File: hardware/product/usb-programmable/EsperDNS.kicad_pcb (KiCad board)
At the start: 4 copper layers, 51 x 48 mm, 53 parts, among them J1 USB_B_Micro, J3 RJ45_Amphenol_RJMG1BD3B8K1ANR, Q1 2N7002, Q2 2N7002, Q3 2N7002, Q4 2N7002, Q5 2N7002, SW1 PTS645VH83-2 LFS, U1 AZ1117EH-3.3TRG1, U2 ESP32-WROOM-32E, U3 LAN8720A, U4 CP2102-GMR_NRND

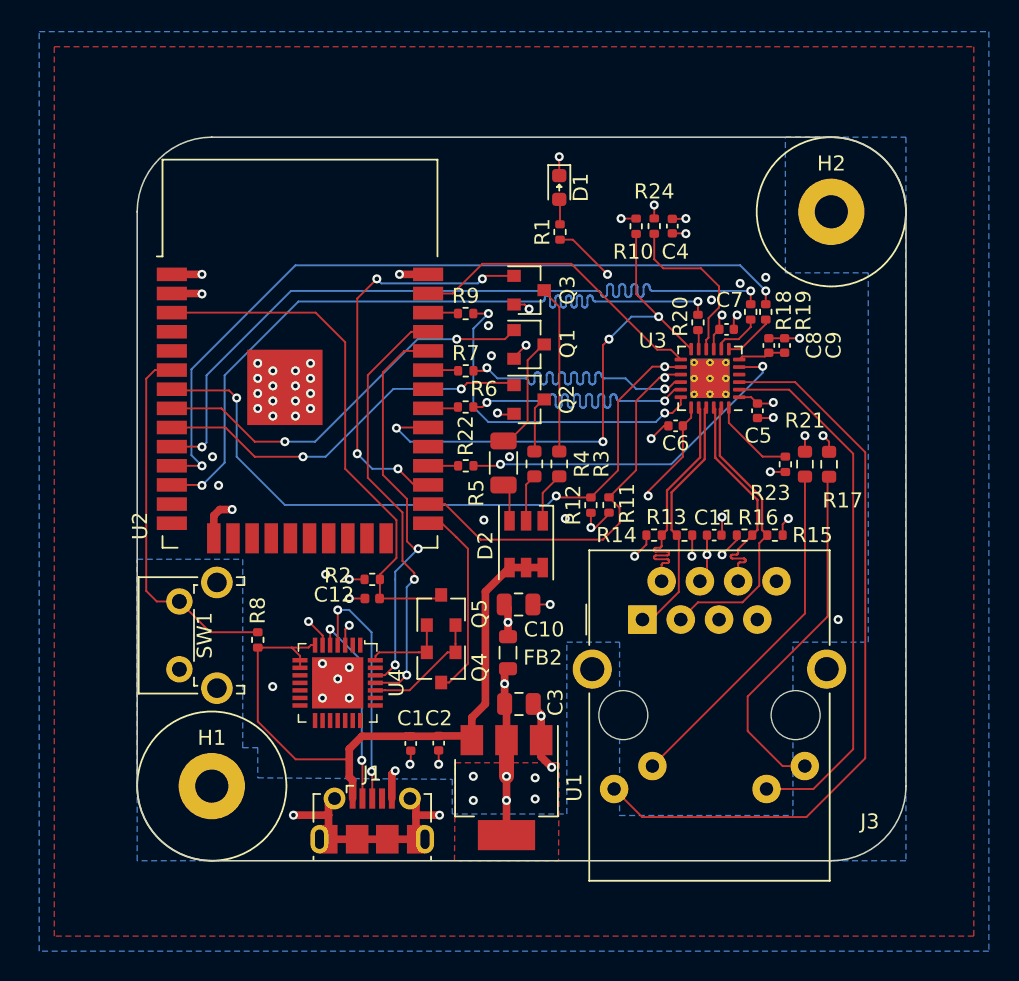
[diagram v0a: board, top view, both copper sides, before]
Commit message: Changed to new PHY
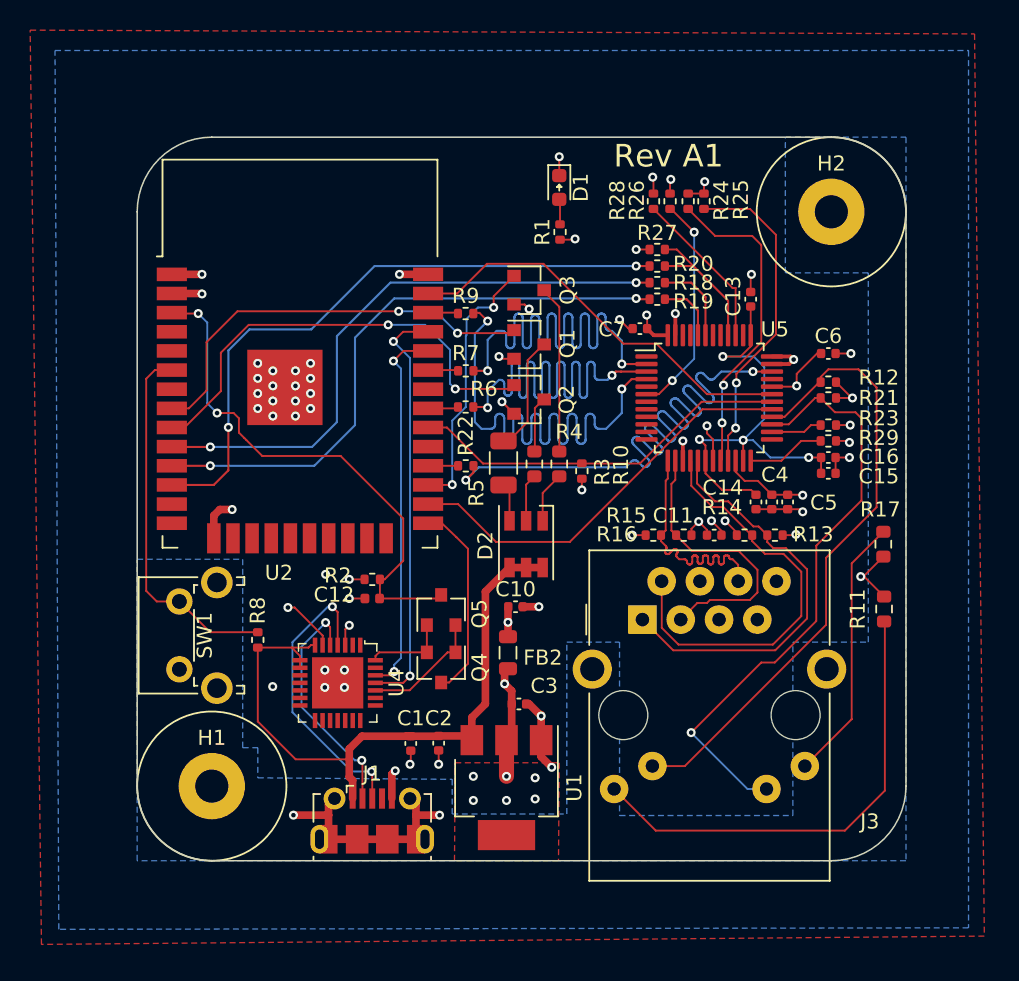
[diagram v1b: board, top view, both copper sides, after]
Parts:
- removed C8: 0.1uF, Capacitor_SMD:C_0402_1005Metric
- removed C9: 1uF, Capacitor_SMD:C_0402_1005Metric
- removed U3: LAN8720A, Package_DFN_QFN:QFN-24-1EP_4x4mm_P0.5mm_EP2.6x2.6mm_ThermalVias
- added C13: 0.1uF, Capacitor_SMD:C_0402_1005Metric, F.Cu at (15.2, -13.2)
- added C14: 0.1uF, Capacitor_SMD:C_0402_1005Metric, F.Cu at (15.6, 0.20)
- added C15: 10uF, Capacitor_SMD:C_0402_1005Metric, F.Cu at (20.4, -1.70)
- added C16: 0.1uF, Capacitor_SMD:C_0402_1005Metric, F.Cu at (20.4, -2.75)
- added R25: 2.2k, Resistor_SMD:R_0402_1005Metric, F.Cu at (12.1, -19.8)
- added R26: 2.2k, Resistor_SMD:R_0402_1005Metric, F.Cu at (8.75, -19.8)
- added R27: 2.2k, Resistor_SMD:R_0402_1005Metric, F.Cu at (9.00, -16.6)
- added R28: 2.2k, Resistor_SMD:R_0402_1005Metric, F.Cu at (9.85, -19.8)
- added R29: 4.87, Resistor_SMD:R_0402_1005Metric, F.Cu at (20.4, -3.85)
- added U5: DP83848C, Package_QFP:LQFP-48_7x7mm_P0.5mm, F.Cu at (12.4, -6.70)
- C10, C3: footprint Capacitor_SMD:C_0805_2012Metric -> Capacitor_SMD:C_0402_1005Metric
- R10, R12, R24: value 10K -> 2.2k
- R11: value 10K -> 270; footprint Resistor_SMD:R_0402_1005Metric -> Resistor_SMD:R_0603_1608Metric
- R21: value 270 -> 2.2k; footprint Resistor_SMD:R_0603_1608Metric -> Resistor_SMD:R_0402_1005Metric
- R23: value 12.1K -> 2.2k
- moved R11 19.5 mm to (24.1, 7.30), turned to 270 degrees
- moved C4 19.5 mm to (16.6, 0.20), turned to 270 degrees
- moved R12 17.7 mm to (20.4, -7.75), turned to 180 degrees
- moved R10 16.6 mm to (4.00, -1.85), turned to 90 degrees
- moved C6 11.2 mm to (20.4, -9.65), turned to 0 degrees
- moved R19 7.25 mm to (9.00, -13.2), turned to 180 degrees
- moved R18 6.50 mm to (9.00, -14.3), turned to 180 degrees
- moved R17 6.41 mm to (24.0, 3.00), turned to 90 degrees
- moved C5 6.37 mm to (17.6, 0.20)
- moved R15 6.05 mm to (10.8, 2.40)
- moved R16 6.05 mm to (8.74, 2.40)
- moved R14 6.00 mm to (14.8, 2.40)
- moved R13 6.00 mm to (16.8, 2.40)
- moved C7 5.75 mm to (7.85, -11.3), turned to 180 degrees
- moved R21 4.66 mm to (20.4, -6.70), turned to 180 degrees
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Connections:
- C6 pad 1: +3.3VA -> +3V3
- J3 pad L2: LED2_nINTSEL -> /LED_SPEED
- J3 pad L3: /LEDG_K -> /LED_LINK
- J3 pad L4: LED1_REGOFF -> /LEDG_A
- R10 pad 1: +3.3VA -> +3V3
- R11 pad 2: nRST -> /LEDG_A
- R12 pad 1: +3.3VA -> +3V3
- R12 pad 2: nINT -> /LED_LINK
- R21 pad 1: /LEDG_K -> +3V3
- R21 pad 2: GND -> /LED_SPEED
- R22 pad 1: CLK50MHZ -> CLK_RMII
- R23 pad 1: /RBIAS -> +3V3
- R23 pad 2: GND -> /LED_ACT
- R24 pad 1: /PHYAD0 -> +3V3
- R24 pad 2: GND -> /RESERVED0
- U2 pad 7: nINT -> Net-(U2-Pad7)
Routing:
- net LED1_REGOFF: track 49.6 -> 0.00 mm
- net nINT: track 45.8 -> 0.00 mm, vias 3 -> 0
- net CLK_RMII: track 0.00 -> 45.1 mm, vias 0 -> 2
- net /LED_LINK: track 0.00 -> 41.5 mm
- net /LED_SPEED: track 0.00 -> 39.8 mm, vias 0 -> 1
- net LED2_nINTSEL: track 35.8 -> 0.00 mm
- net /LEDG_A: track 0.00 -> 31.4 mm
- net /PFB: track 0.00 -> 30.6 mm, vias 0 -> 4
- net CLK50MHZ: track 23.9 -> 0.00 mm, vias 2 -> 0
- net /LEDG_K: track 23.7 -> 0.00 mm
- net /RESERVED1: track 0.00 -> 21.8 mm, vias 0 -> 2
- net /RESERVED0: track 0.00 -> 21.3 mm, vias 0 -> 2
- net TXD1: track 22.8 -> 41.0 mm
- net TXEN: track 22.0 -> 39.9 mm
- net TXD0: track 22.1 -> 38.8 mm
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- added copper zone on In2.Cu, net +3.3VA
- added copper zone on B.Cu, net +3V3
- added copper zone on In1.Cu, net GND
- added copper zone on In2.Cu, net GND
- removed copper zone on Pwr, net +3.3VA
- removed copper zone on Pwr, net +3V3
- removed copper zone on B.Cu, net GND
- removed copper zone on Gnd, net GND
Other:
- board text added: "Rev A1"
